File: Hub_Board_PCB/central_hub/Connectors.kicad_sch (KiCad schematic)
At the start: 15 parts, among them J3 Screw_Terminal_01x08, J4 Screw_Terminal_01x08, J5 CSP-USC16-TR, J6 Screw_Terminal_01x04, J7 Conn_01x03, J8 Conn_01x02

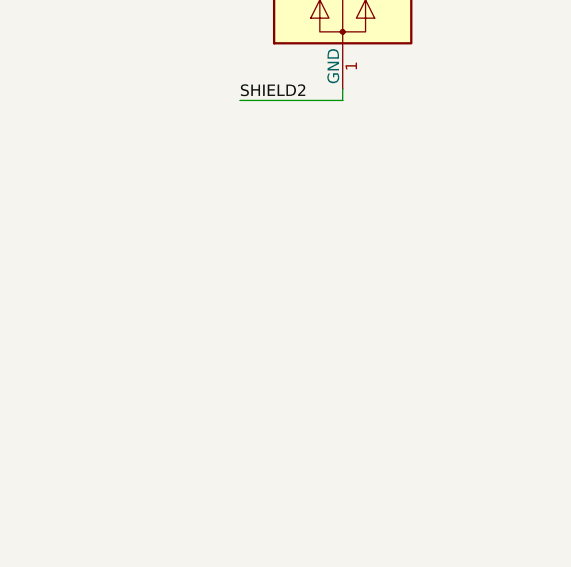
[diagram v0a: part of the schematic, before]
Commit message: Central hub layout first draft (+ some changes to motor driver)
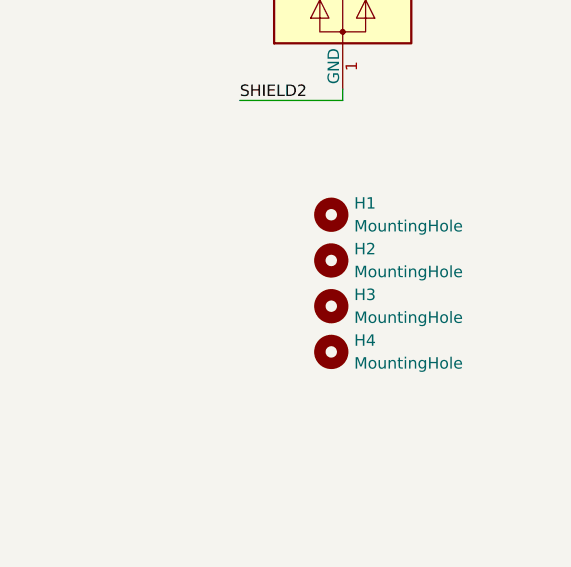
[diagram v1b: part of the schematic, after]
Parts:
- added H1, H2, H3, H4: MountingHole, MountingHole:MountingHole_3mm, symbol Mechanical:MountingHole
- C20, C21, C22: footprint (none) -> Capacitor_SMD:C_0603_1608Metric
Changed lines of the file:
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@@
+    )
+  )
+  (symbol (lib_id "Mechanical:MountingHole") (at 231.14 134.62 0) (unit 1)
+    (in_bom yes) (on_board yes) (dnp no) (fields_autoplaced)
+    (property "Reference" "H3" (at 233.68 133.35 0)
+      (effects (font (size 1.27 1.27)) (justify left))
+    )
+    (property "Value" "MountingHole" (at 233.68 135.89 0)
+      (effects (font (size 1.27 1.27)) (justify left))
+    )
+    (property "Footprint" "MountingHole:MountingHole_3mm" (at 231.14 134.62 0)
+      (effects (font (size 1.27 1.27)) hide)
+    )
+    (property "Datasheet" "~" (at 231.14 134.62 0)
+      (effects (font (size 1.27 1.27)) hide)
+    )
+    (instances
+      (project "central_hub"
+        (path "/0d9ec66e-0fbf-4d12-9b83-adf78971a00b/8e53aed1-21e6-440d-aae4-1b5509ec346a"
+          (reference "H3") (unit 1)
+        )
+      )
     )
   )
@@
       (effects (font (size 1.27 1.27)) (justify left))
     )
-    (property "Footprint" "" (at 54.3052 110.49 0)
+    (property "Footprint" "Capacitor_SMD:C_0603_1608Metric" (at 54.3052 110.49 0)
       (effects (font (size 1.27 1.27)) hide)
     )
@@
         (path "/0d9ec66e-0fbf-4d12-9b83-adf78971a00b/8e53aed1-21e6-440d-aae4-1b5509ec346a"
           (reference "C20") (unit 1)
+        )
+      )
+    )
+  )
+  (symbol (lib_id "Mechanical:MountingHole") (at 231.14 124.46 0) (unit 1)
+    (in_bom yes) (on_board yes) (dnp no) (fields_autoplaced)
+    (property "Reference" "H1" (at 233.68 123.19 0)
+      (effects (font (size 1.27 1.27)) (justify left))
+    )
+    (property "Value" "MountingHole" (at 233.68 125.73 0)
+      (effects (font (size 1.27 1.27)) (justify left))
+    )
+    (property "Footprint" "MountingHole:MountingHole_3mm" (at 231.14 124.46 0)
+      (effects (font (size 1.27 1.27)) hide)
+    )
+    (property "Datasheet" "~" (at 231.14 124.46 0)
+      (effects (font (size 1.27 1.27)) hide)
+    )
+    (instances
+      (project "central_hub"
+        (path "/0d9ec66e-0fbf-4d12-9b83-adf78971a00b/8e53aed1-21e6-440d-aae4-1b5509ec346a"
+          (reference "H1") (unit 1)
         )
       )
@@
     )
   )
+  (symbol (lib_id "Mechanical:MountingHole") (at 231.14 129.54 0) (unit 1)
+    (in_bom yes) (on_board yes) (dnp no) (fields_autoplaced)
+    (property "Reference" "H2" (at 233.68 128.27 0)
+      (effects (font (size 1.27 1.27)) (justify left))
+    )
+    (property "Value" "MountingHole" (at 233.68 130.81 0)
+      (effects (font (size 1.27 1.27)) (justify left))
+    )
+    (property "Footprint" "MountingHole:MountingHole_3mm" (at 231.14 129.54 0)
+      (effects (font (size 1.27 1.27)) hide)
+    )
+    (property "Datasheet" "~" (at 231.14 129.54 0)
+      (effects (font (size 1.27 1.27)) hide)
+    )
+    (instances
+      (project "central_hub"
+        (path "/0d9ec66e-0fbf-4d12-9b83-adf78971a00b/8e53aed1-21e6-440d-aae4-1b5509ec346a"
+          (reference "H2") (unit 1)
+        )
+      )
+    )
+  )
   (symbol (lib_id "Device:C") (at 66.04 106.68 0) (unit 1)
     (in_bom yes) (on_board yes) (dnp yes) (fields_autoplaced)
@@
       (effects (font (size 1.27 1.27)) (justify left))
     )
-    (property "Footprint" "" (at 67.0052 110.49 0)
+    (property "Footprint" "Capacitor_SMD:C_0603_1608Metric" (at 67.0052 110.49 0)
       (effects (font (size 1.27 1.27)) hide)
     )
@@
       (effects (font (size 1.27 1.27)) (justify left))
     )
-    (property "Footprint" "" (at 79.7052 110.49 0)
+    (property "Footprint" "Capacitor_SMD:C_0603_1608Metric" (at 79.7052 110.49 0)
       (effects (font (size 1.27 1.27)) hide)
     )
@@
         )
       )
+    )
+  )
+  (symbol (lib_id "Mechanical:MountingHole") (at 231.14 139.7 0) (unit 1)
+    (in_bom yes) (on_board yes) (dnp no) (fields_autoplaced)
+    (property "Reference" "H4" (at 233.68 138.43 0)
+      (effects (font (size 1.27 1.27)) (justify left))
+    )
+    (property "Value" "MountingHole" (at 233.68 140.97 0)
+      (effects (font (size 1.27 1.27)) (justify left))
+    )
+    (property "Footprint" "MountingHole:MountingHole_3mm" (at 231.14 139.7 0)
+      (effects (font (size 1.27 1.27)) hide)
+    )
+    (property "Datasheet" "~" (at 231.14 139.7 0)
+      (effects (font (size 1.27 1.27)) hide)
+    )
+    (instances
+      (project "central_hub"
+        (path "/0d9ec66e-0fbf-4d12-9b83-adf78971a00b/8e53aed1-21e6-440d-aae4-1b5509ec346a"
+          (reference "H4") (unit 1)
+        )
+      )

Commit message: Central Hub USB changes
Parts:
- removed TP? (x2): TestPoint, TestPoint:TestPoint_Pad_D1.0mm, symbol Connector:TestPoint
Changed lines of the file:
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@@
-    )
-  )
-  (symbol (lib_id "Connector:TestPoint") (at 93.98 148.59 270) (mirror x) (unit 1)
-    (in_bom yes) (on_board yes) (dnp no)
-    (property "Reference" "TP?" (at 101.6 148.59 90)
-      (effects (font (size 1.27 1.27)))
-    )
-    (property "Value" "TestPoint" (at 97.282 146.05 90)
-      (effects (font (size 1.27 1.27)) hide)
-    )
-    (property "Footprint" "TestPoint:TestPoint_Pad_D1.0mm" (at 93.98 143.51 0)
-      (effects (font (size 1.27 1.27)) hide)
-    )
-    (property "Datasheet" "~" (at 93.98 143.51 0)
-      (effects (font (size 1.27 1.27)) hide)
-    )
-    (pin "1")
-    (instances
-      (project "central_hub"
-        (path "/0d9ec66e-0fbf-4d12-9b83-adf78971a00b"
-          (reference "TP?") (unit 1)
-        )
-        (path "/0d9ec66e-0fbf-4d12-9b83-adf78971a00b/4fb60496-ee10-4e45-a75e-a49c2c8afc68"
-          (reference "TP?") (unit 1)
-        )
-        (path "/0d9ec66e-0fbf-4d12-9b83-adf78971a00b/8e53aed1-21e6-440d-aae4-1b5509ec346a"
-          (reference "TP8") (unit 1)
-        )
-      )
-      (project "motor_board_pcb"
-        (path "/4ad82a24-c992-45c9-b523-12e12bcd6ced/996060af-581e-425f-9e10-26ee39d5a960"
-          (reference "TP8") (unit 1)
-        )
-      )
     )
   )
@@
         )
       )
-    )
-  )
-  (symbol (lib_id "Connector:TestPoint") (at 93.98 146.05 270) (mirror x) (unit 1)
-    (in_bom yes) (on_board yes) (dnp no)
-    (property "Reference" "TP?" (at 101.6 146.05 90)
-      (effects (font (size 1.27 1.27)))
-    )
-    (property "Value" "TestPoint" (at 97.282 143.51 90)
-      (effects (font (size 1.27 1.27)) hide)
-    )
-    (property "Footprint" "TestPoint:TestPoint_Pad_D1.0mm" (at 93.98 140.97 0)
-      (effects (font (size 1.27 1.27)) hide)
-    )
-    (property "Datasheet" "~" (at 93.98 140.97 0)
-      (effects (font (size 1.27 1.27)) hide)
-    )
-    (pin "1")
-    (instances
-      (project "central_hub"
-        (path "/0d9ec66e-0fbf-4d12-9b83-adf78971a00b"
-          (reference "TP?") (unit 1)
-        )
-        (path "/0d9ec66e-0fbf-4d12-9b83-adf78971a00b/4fb60496-ee10-4e45-a75e-a49c2c8afc68"
-          (reference "TP?") (unit 1)
-        )
-        (path "/0d9ec66e-0fbf-4d12-9b83-adf78971a00b/8e53aed1-21e6-440d-aae4-1b5509ec346a"
-          (reference "TP7") (unit 1)
-        )
-      )
-      (project "motor_board_pcb"
-        (path "/4ad82a24-c992-45c9-b523-12e12bcd6ced/996060af-581e-425f-9e10-26ee39d5a960"
-          (reference "TP7") (unit 1)
-        )
-      )

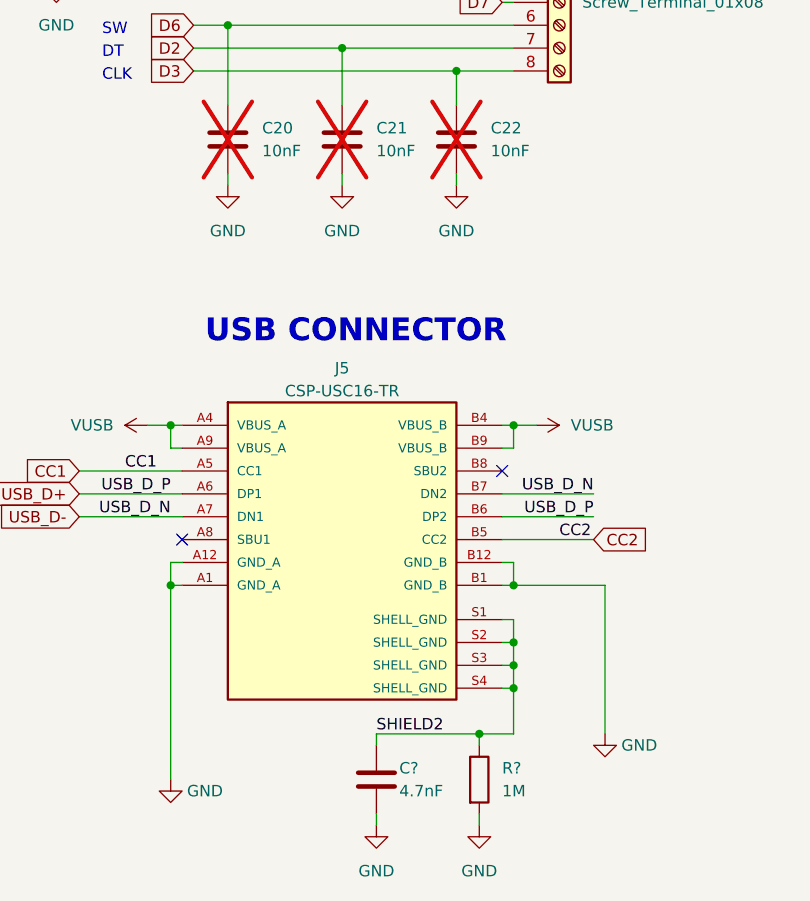
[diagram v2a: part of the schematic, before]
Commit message: - added footprint labels to schematic
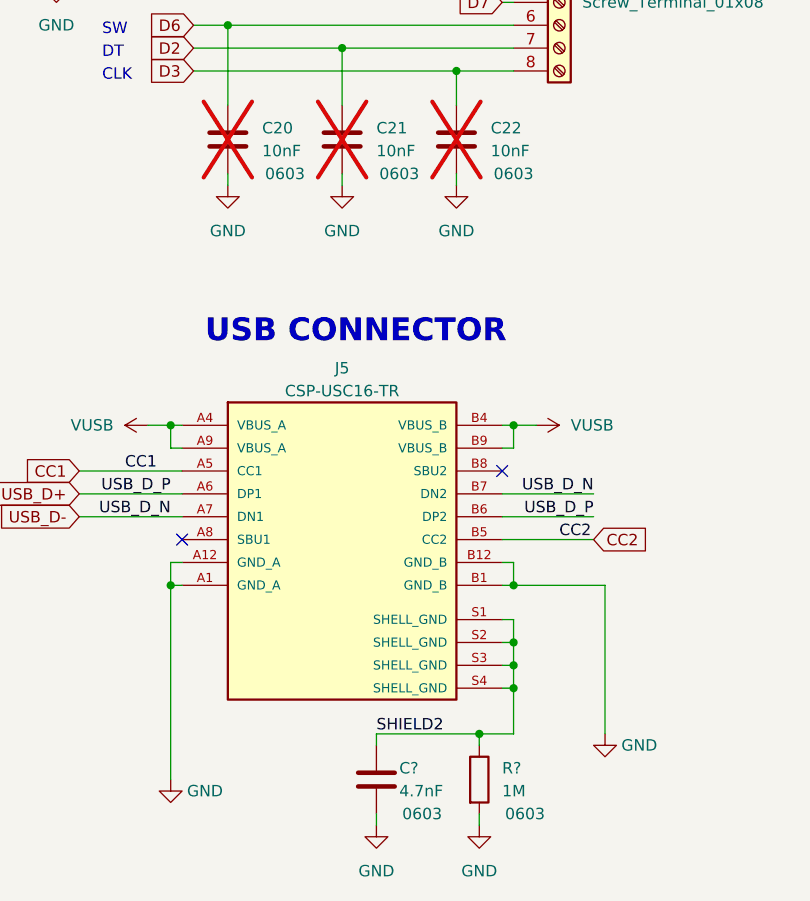
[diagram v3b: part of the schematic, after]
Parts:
- C20, C21, C22, C?, R?: FP (none) -> 0603
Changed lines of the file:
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@@
   )
   (symbol (lib_id "Device:C") (at 53.34 106.68 0) (unit 1)
-    (in_bom yes) (on_board yes) (dnp yes) (fields_autoplaced)
+    (in_bom yes) (on_board yes) (dnp yes)
     (property "Reference" "C20" (at 57.15 105.41 0)
       (effects (font (size 1.27 1.27)) (justify left))
@@
     (property "Datasheet" "~" (at 53.34 106.68 0)
       (effects (font (size 1.27 1.27)) hide)
+    )
+    (property "FP" "0603" (at 59.69 110.49 0)
+      (effects (font (size 1.27 1.27)))
     )
     (pin "1")
@@
   )
   (symbol (lib_id "Device:C") (at 66.04 106.68 0) (unit 1)
-    (in_bom yes) (on_board yes) (dnp yes) (fields_autoplaced)
+    (in_bom yes) (on_board yes) (dnp yes)
     (property "Reference" "C21" (at 69.85 105.41 0)
       (effects (font (size 1.27 1.27)) (justify left))
@@
       (effects (font (size 1.27 1.27)) hide)
     )
+    (property "FP" "0603" (at 72.39 110.49 0)
+      (effects (font (size 1.27 1.27)))
+    )
     (pin "1")
     (pin "2")
@@
   )
   (symbol (lib_id "Device:C") (at 78.74 106.68 0) (unit 1)
-    (in_bom yes) (on_board yes) (dnp yes) (fields_autoplaced)
+    (in_bom yes) (on_board yes) (dnp yes)
     (property "Reference" "C22" (at 82.55 105.41 0)
       (effects (font (size 1.27 1.27)) (justify left))
@@
     (property "Datasheet" "~" (at 78.74 106.68 0)
       (effects (font (size 1.27 1.27)) hide)
+    )
+    (property "FP" "0603" (at 85.09 110.49 0)
+      (effects (font (size 1.27 1.27)))
     )
     (pin "1")
@@
   )
   (symbol (lib_id "Device:R") (at 81.28 177.8 0) (unit 1)
-    (in_bom yes) (on_board yes) (dnp no) (fields_autoplaced)
+    (in_bom yes) (on_board yes) (dnp no)
     (property "Reference" "R?" (at 83.82 176.53 0)
       (effects (font (size 1.27 1.27)) (justify left))
@@
     (property "Datasheet" "~" (at 81.28 177.8 0)
       (effects (font (size 1.27 1.27)) hide)
+    )
+    (property "FP" "0603" (at 86.36 181.61 0)
+      (effects (font (size 1.27 1.27)))
     )
     (pin "1")
@@
       (effects (font (size 1.27 1.27)) hide)
     )
-    (pin "1")
+    (property "FP" "0603" (at 74.93 181.61 0)
+      (effects (font (size 1.27 1.27)))
+    )
+    (pin "1")
